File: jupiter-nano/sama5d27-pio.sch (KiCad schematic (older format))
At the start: 2 parts, among them U1 ATSAMA5D27C-LD1G-CU

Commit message: added at24csw080 I2C EEPROM UUID chip
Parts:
- renumbered R13 to R16
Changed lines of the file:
@@
 ADTRG-IRQ
 $Comp
-L Device:R_Small R13
+L Device:R_Small R16
 U 1 1 600D6DFE
 P 9100 1050
-F 0 "R13" H 9159 1096 50  0000 L CNN
+F 0 "R16" H 9159 1096 50  0000 L CNN
 F 1 "100K" H 9159 1005 50  0000 L CNN
 F 2 "" H 9100 1050 50  0001 C CNN
@@
 	9100 950  9100 850
 $Comp
-L power:GND #PWR024
+L power:GND #PWR025
 U 1 1 600DB627
 P 9100 850
-F 0 "#PWR024" H 9100 600 50  0001 C CNN
+F 0 "#PWR025" H 9100 600 50  0001 C CNN
 F 1 "GND" H 9105 677 50  0000 C CNN
 F 2 "" H 9100 850 50  0001 C CNN

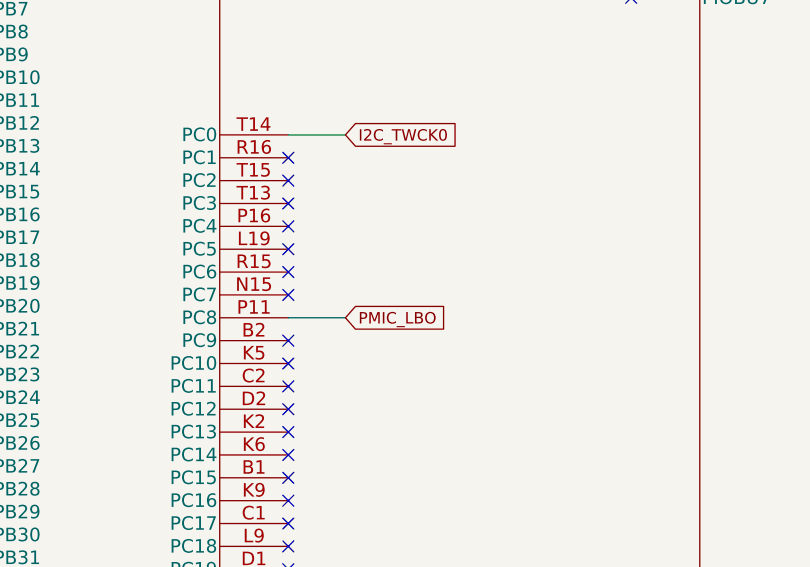
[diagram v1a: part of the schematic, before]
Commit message: reorganized connector sheet
- and library location change
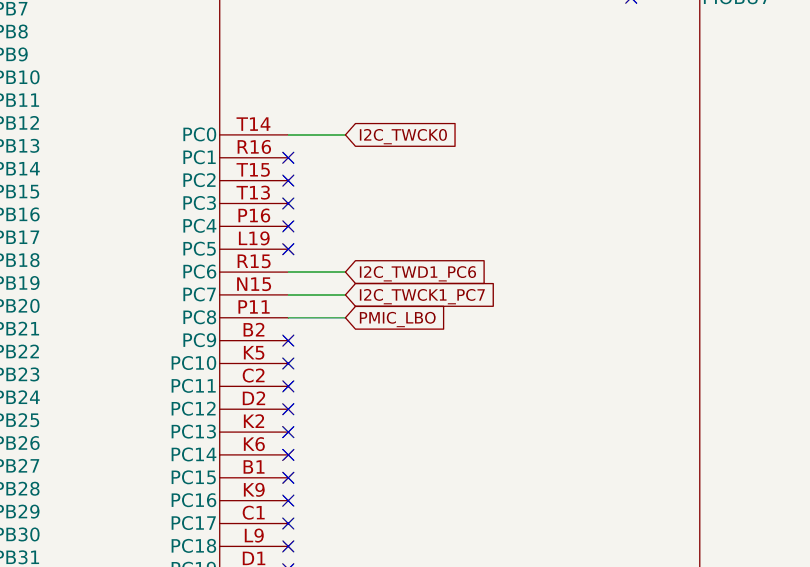
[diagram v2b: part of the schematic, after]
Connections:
- net I2C_TWCK1_PC7: now reaches U1.N15 (PC7)
- net I2C_TWD1_PC6: now reaches U1.R15 (PC6)
- no-connect marks 96 -> 94
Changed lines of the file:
@@
 NoConn ~ 5750 3050
 NoConn ~ 5750 3150
-NoConn ~ 5750 3250
-NoConn ~ 5750 3350
 NoConn ~ 5750 3550
 NoConn ~ 5750 3650
@@
 NoConn ~ 9050 2100
 NoConn ~ 9050 2000
+Text GLabel 6000 3250 2    50   Input ~ 0
+I2C_TWD1_PC6
+Text GLabel 6000 3350 2    50   Input ~ 0
+I2C_TWCK1_PC7
+Wire Wire Line
+	5750 3250 6000 3250
+Wire Wire Line
+	5750 3350 6000 3350
 $EndSCHEMATC
